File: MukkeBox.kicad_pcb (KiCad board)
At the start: 4 copper layers, 291 parts, among them J101 ST_Link_V2_10P, J102 Jumper, J103 Jumper, J104 Jumper, J105 Jumper, J106 Jumper, J107 PinHeader, J108 PinHeader, J201 TB001-500-07BE CUI_Devices, J401 TB001-500-02BE CUI_Devices, J501 TB001-500-04BE CUI_Devices, J601 Conn_01x03_Female, J602 Conn_02x01, J801 Conn_01x04, J802 Conn_01x04, Q101 NTK3043N, Q201 NTD14N03RT4G, Q202 NTD14N03RT4G, Q203 NTD14N03RT4G, Q301 MMBT2222LT1G, Q302 TK7R7P10PL, Q401 NTK3043N, Q402 FDD4685-F085, SW101 Rotary_Encoder_Switch, SW501 DS04-254-2-02BK-SMT, U101 TPS7B82-Q1, U102 STM32F030C6Tx_MukkeBox, U201 BQ76920, U202 BQ76200, U301 L7812, U302 UC3843_SOIC8, U401 MAX1873TEEE, U402 PC827, U501 TDA7498L, U601 XC6216C, U602 TDA7418, U701 XS3868, U801 MCP23017_SO, Y101 FOXSDLF/080-20

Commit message: Balancer geplaced
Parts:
- J401: moved to F.Cu
- moved J201 356.0 mm to (38.4, 114.2), turned to 90 degrees
- moved C203 355.9 mm to (47.3, 105.9), turned to 180 degrees
- moved R210 350.6 mm to (59.7, 110.9)
- moved D201 348.4 mm to (70.0, 109.6)
- moved C212 345.8 mm to (77.7, 103.1), turned to 270 degrees
- moved R215 345.0 mm to (90.5, 121.1)
- moved R206 341.3 mm to (59.1, 116.7)
- moved R205 341.0 mm to (47.3, 115.4)
- moved Q202 340.5 mm to (90.7, 109.9), turned to 90 degrees
- moved R207 338.6 mm to (40.0, 119.8), turned to 180 degrees
- moved C207 335.8 mm to (61.0, 115.0), turned to 180 degrees
- moved C204 334.6 mm to (47.3, 110.9), turned to 180 degrees
- moved R204 334.4 mm to (47.3, 109.2), turned to 180 degrees
- moved C205 334.0 mm to (47.3, 113.7), turned to 180 degrees
- moved R208 333.8 mm to (62.8, 116.7), turned to 180 degrees
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
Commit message: Step Up geplaced
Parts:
- moved R306 379.7 mm to (203.9, 60.2), turned to 90 degrees
- moved HS302 365.9 mm to (201.4, 45.2)
- moved R305 360.4 mm to (177.5, 63.9)
- moved R303 358.5 mm to (190.1, 60.6)
- moved C305 357.6 mm to (225.4, 35.7), turned to 270 degrees
- moved R302 356.3 mm to (185.3, 53.5), turned to 90 degrees
- moved R304 354.5 mm to (177.5, 62.1), turned to 180 degrees
- moved C306 353.4 mm to (190.1, 58.1)
- moved L301 351.9 mm to (172.9, 30.8)
- moved HS301 351.3 mm to (201.4, 24.2)
- moved R308 349.8 mm to (177.5, 58.9), turned to 180 degrees
- moved C302 347.0 mm to (183.7, 65.1)
- moved Q302 346.2 mm to (201.4, 48.6), turned to 90 degrees
- moved R301 345.1 mm to (177.5, 55.5), turned to 180 degrees
- moved Q301 343.5 mm to (182.1, 53.6)
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
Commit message: Alle Parts geplaced: Dimension der Platine 200x105qmm. TODO Anzeige überarbeiten
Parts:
- added C307: 560uF 50V, Capacitor_THT:CP_Radial_D12.5mm_P5.00mm, B.Cu at (117.1, 54.1)
- added C308: 560uF 50V, Capacitor_THT:CP_Radial_D12.5mm_P5.00mm, B.Cu at (175.1, 54.1)
- C301: value 1000u35V EEV-FK1V102V -> 560uF 50V; footprint Capacitor_SMD:CP_Elec_16x17.5 -> Capacitor_THT:CP_Radial_D12.5mm_P5.00mm; moved to B.Cu
- C305: value 1000u60V EEV-FK1V102V -> 560uF 50V; footprint Capacitor_SMD:CP_Elec_16x17.5 -> Capacitor_THT:CP_Radial_D12.5mm_P5.00mm; moved to B.Cu
- C525, C530, C531, C532, L501, L502, L503, L504: moved to B.Cu
- U102: footprint Package_QFP:LQFP-64_10x10mm_P0.5mm -> Package_QFP:LQFP-48_7x7mm_P0.5mm
- Y101: footprint Crystal:Crystal_SMD_HC49-SD_HandSoldering -> Crystal:Crystal_SMD_HC49-SD
- moved J501 278.4 mm to (240.8, 60.3), turned to 270 degrees
- moved R510 267.3 mm to (235.2, 88.6), turned to 90 degrees
- moved R511 267.2 mm to (234.9, 76.0), turned to 90 degrees
- moved U601 258.6 mm to (199.6, 117.1), turned to 180 degrees
- moved C525 258.4 mm to (211.4, 82.6), turned to 90 degrees
- moved C601 257.8 mm to (204.7, 118.1), turned to 180 degrees
- moved R601 255.4 mm to (194.8, 115.8), turned to 180 degrees
- moved R602 255.4 mm to (194.8, 119.1), turned to 180 degrees
- moved C612 254.9 mm to (185.9, 111.5), turned to 180 degrees
- moved C602 254.7 mm to (188.0, 117.3), turned to 270 degrees
- moved C528 254.6 mm to (235.2, 84.1), turned to 90 degrees
- moved C529 254.1 mm to (235.2, 80.5), turned to 90 degrees
- moved L503 253.2 mm to (224.8, 87.9)
- moved C523 251.9 mm to (233.5, 84.1), turned to 90 degrees
- moved R808 251.6 mm to (216.9, 137.7), turned to 180 degrees
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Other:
- board outline added: 200 x 105 mm

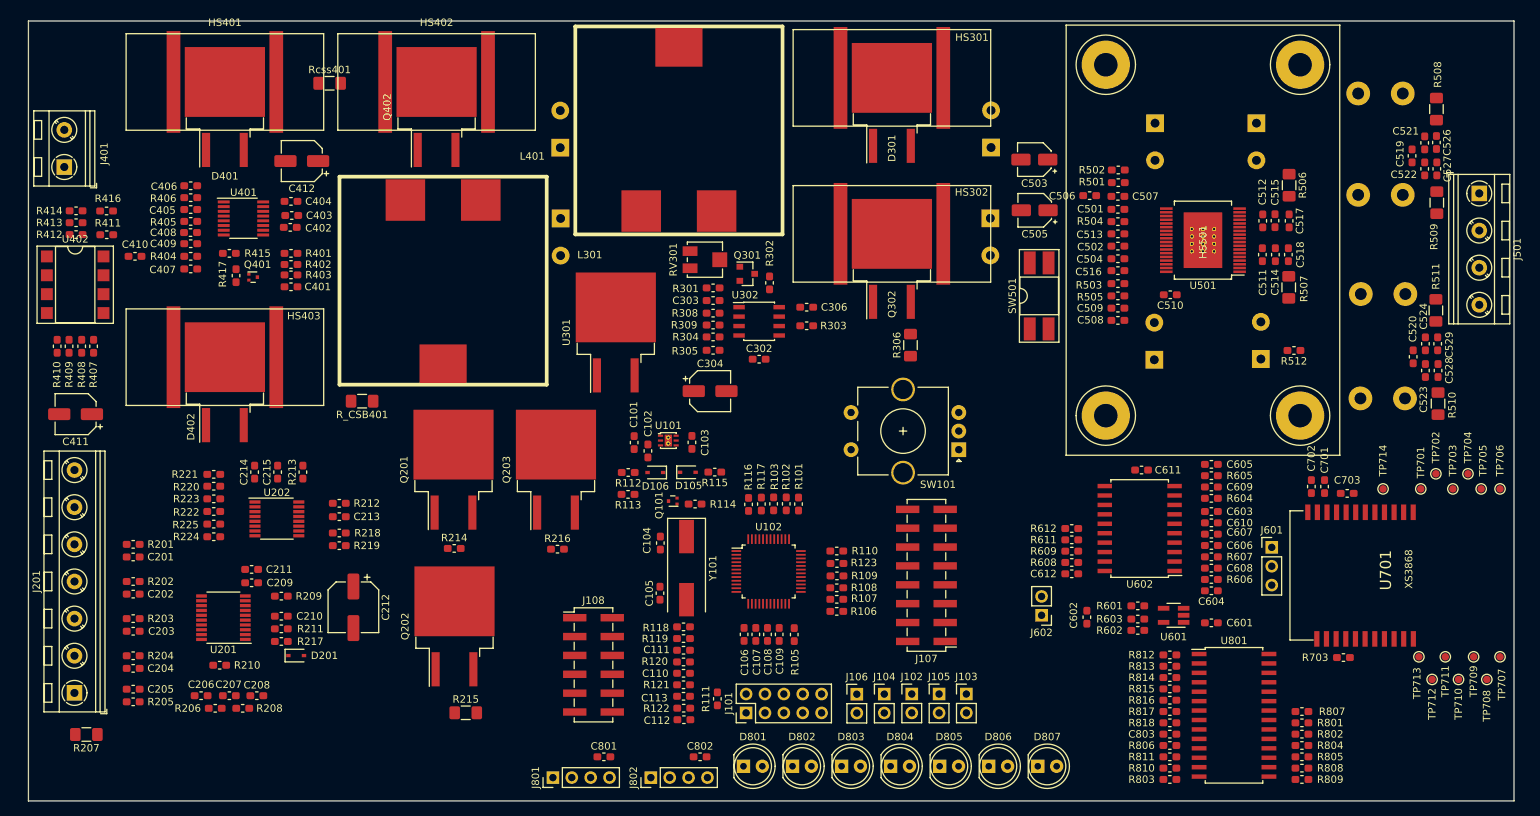
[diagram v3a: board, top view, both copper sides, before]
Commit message: Mountingholes und Heatsinks hinzugefügt
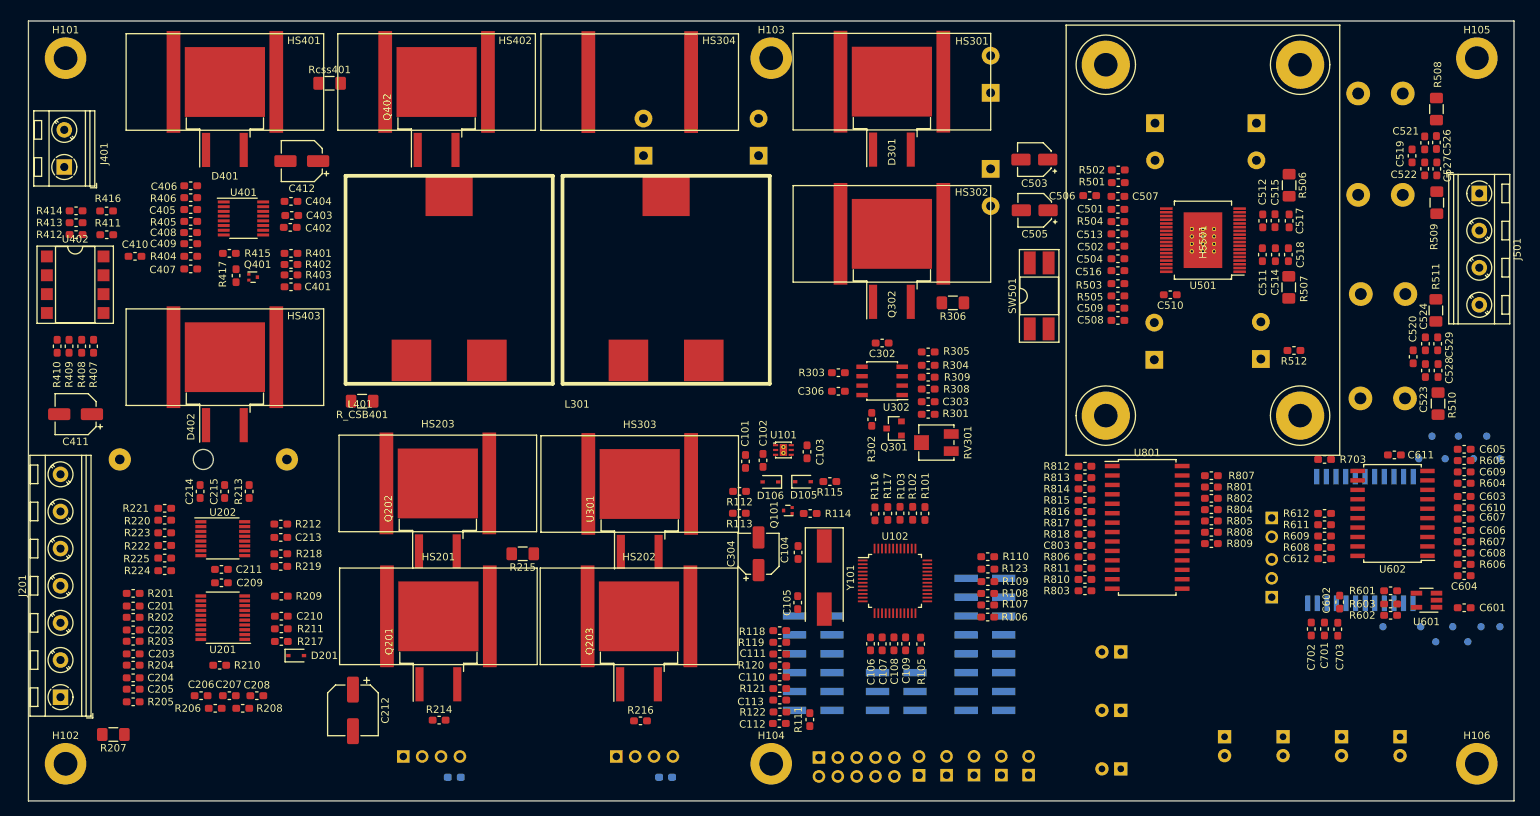
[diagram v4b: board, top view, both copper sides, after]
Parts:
- removed SW101: Rotary_Encoder_Switch, Rotary_Encoder:RotaryEncoder_Alps_EC11E-Switch_Vertical_H20mm_CircularMountingHoles
- added F201: Fuse, Fuse:Fuseholder_Cylinder-5x20mm_Schurter_0031_8201_Horizontal_Open, B.Cu at (80.3, 96.1)
- added H101: MountingHole_Pad, MountingHole:MountingHole_3.2mm_M3_DIN965_Pad, F.Cu at (50.5, 42.1)
- added H102: MountingHole_Pad, MountingHole:MountingHole_3.2mm_M3_DIN965_Pad, F.Cu at (50.5, 137.1)
- added H103: MountingHole_Pad, MountingHole:MountingHole_3.2mm_M3_DIN965_Pad, F.Cu at (145.5, 42.1)
- added H104: MountingHole_Pad, MountingHole:MountingHole_3.2mm_M3_DIN965_Pad, F.Cu at (145.5, 137.1)
- added H105: MountingHole_Pad, MountingHole:MountingHole_3.2mm_M3_DIN965_Pad, F.Cu at (240.5, 42.1)
- added H106: MountingHole_Pad, MountingHole:MountingHole_3.2mm_M3_DIN965_Pad, F.Cu at (240.5, 137.1)
- added HS201: Heatsink_Pad, Heatsink:Heatsink_AAVID_573300D00010G_TO-263, F.Cu at (100.7, 117.2)
- added HS202: Heatsink_Pad, Heatsink:Heatsink_AAVID_573300D00010G_TO-263, F.Cu at (127.7, 117.2)
- added HS203: Heatsink_Pad, Heatsink:Heatsink_AAVID_573300D00010G_TO-263, F.Cu at (100.6, 99.3)
- added HS303: Heatsink_Pad, Heatsink:Heatsink_AAVID_573300D00010G_TO-263, F.Cu at (127.8, 99.4)
- added HS304: Heatsink_Pad, Heatsink:Heatsink_AAVID_573300D00010G_TO-263, F.Cu at (127.8, 45.3)
- added J109: PinHeader, Connector_PinHeader_2.54mm:PinHeader_2x03_P2.54mm_Vertical_SMD, B.Cu at (162.3, 127.4)
- C801, C802, D801, D802, D803, D804, D805, D806, D807, J101, J102, J103, J104, J105, J106, J107, J108, J601, J602, J801, J802, TP701, TP702, TP703, TP704, TP705, TP706, TP707, TP708, TP709, TP710, TP711, TP712, TP713, TP714, U701: moved to B.Cu
- moved D801 88.5 mm to (230.1, 133.4), turned to 270 degrees
- moved D802 74.0 mm to (222.2, 133.4), turned to 270 degrees
- moved D803 59.6 mm to (214.4, 133.4), turned to 270 degrees
- moved D804 45.1 mm to (206.5, 133.4), turned to 270 degrees
- moved RV301 39.7 mm to (167.7, 93.8), turned to 270 degrees
- moved C601 34.1 mm to (238.8, 116.1)
- moved C602 34.1 mm to (222.0, 115.3)
- moved C603 34.1 mm to (238.8, 101.1)
- moved C604 34.1 mm to (238.8, 111.8)
- moved C605 34.1 mm to (238.8, 94.7)
- moved C606 34.1 mm to (238.8, 105.7)
- moved C607 34.1 mm to (238.8, 104.1)
- moved C608 34.1 mm to (238.8, 108.7)
- moved C609 34.1 mm to (238.8, 97.8)
- moved C610 34.1 mm to (238.8, 102.6)
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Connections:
- J201 pad 5: BATTERY+ -> /01_BMS/CELL4_SENSE
- R201 pad 2: BATTERY+ -> /01_BMS/CELL4_SENSE

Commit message: fertig zum routen
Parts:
- removed J102, J103, J105, J106: Jumper, Connector_PinHeader_2.54mm:PinHeader_1x02_P2.54mm_Vertical
- added J301: Conn_02x04_Odd_Even, Connector_PinHeader_2.54mm:PinHeader_2x04_P2.54mm_Vertical, B.Cu at (113.5, 54.3)
- added J302: Conn_02x04_Odd_Even, Connector_PinHeader_2.54mm:PinHeader_2x04_P2.54mm_Vertical, B.Cu at (186.5, 48.3)
- HS201, HS202, HS203, HS301, HS302, HS303, HS304: value Heatsink_Pad -> 573300D00000G
- J104: value Jumper -> Conn_02x05_Odd_Even; footprint Connector_PinHeader_2.54mm:PinHeader_1x02_P2.54mm_Vertical -> Connector_PinHeader_2.54mm:PinHeader_2x05_P2.54mm_Vertical_SMD
- J601: footprint Connector_PinHeader_2.54mm:PinHeader_1x03_P2.54mm_Vertical -> Connector_PinHeader_2.54mm:PinHeader_1x03_P2.54mm_Vertical_SMD_Pin1Left
- J602: footprint Connector_PinHeader_2.54mm:PinHeader_1x02_P2.54mm_Vertical -> Connector_PinHeader_2.54mm:PinHeader_1x02_P2.54mm_Vertical_SMD_Pin1Left
- J801: value Conn_01x04 -> Conn_01x05; footprint Connector_PinHeader_2.54mm:PinHeader_1x04_P2.54mm_Vertical -> Connector:1x04_P2.54mm_1.3OLED
- moved J801 114.6 mm to (208.2, 113.3), turned to 180 degrees
- moved J104 36.4 mm to (174.2, 102.6)
- moved D805 32.2 mm to (202.9, 107.3), turned to 270 degrees
- moved D806 22.8 mm to (195.0, 107.3), turned to 270 degrees
- moved R809 22.1 mm to (203.2, 129.4)
- moved C803 22.1 mm to (186.2, 129.7)
- moved R801 22.1 mm to (203.2, 121.8)
- moved R802 22.1 mm to (203.2, 123.3)
- moved R803 22.1 mm to (186.2, 135.8)
- moved R804 22.1 mm to (203.2, 124.9)
- moved R805 22.1 mm to (203.2, 126.4)
- moved R806 22.1 mm to (186.2, 131.2)
- moved R807 22.1 mm to (203.2, 120.3)
- moved R808 22.1 mm to (203.2, 127.9)
- moved R810 22.1 mm to (186.2, 134.3)
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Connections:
- C301 pad 1: SYSTEM_LOAD -> Net-(C301-Pad1)
- C305 pad 1: POWER_AMP -> Net-(C305-Pad1)
- C307 pad 1: SYSTEM_LOAD -> Net-(C301-Pad1)
- C308 pad 1: POWER_AMP -> Net-(C305-Pad1)
- C801 pad 1: +3V3 -> GND
- C801 pad 2: GND -> +3V3
- D301 pad 2: POWER_AMP -> Net-(C305-Pad1)
- HS301 pad 1: POWER_AMP -> Net-(C305-Pad1)
- J101 pad 7: Net-(J101-Pad7) -> /ST_Link_3V3
- J101 pad 8: Net-(J101-Pad7) -> /ST_Link_3V3
- J401 pad 1: GNDPWR -> GND
- J801 pad 1: SDA -> GND
- J801 pad 2: SCL -> +3V3
- J801 pad 3: +3V3 -> SCL
- J801 pad 4: GND -> SDA
- L301 pad 1: SYSTEM_LOAD -> Net-(C301-Pad1)
- R304 pad 2: SYSTEM_LOAD -> Net-(C301-Pad1)
- RV301 pad 1: POWER_AMP -> Net-(C305-Pad1)
- U102 pad 22: Net-(J102-Pad1) -> Net-(J104-Pad3)
- U102 pad 30: Net-(J105-Pad1) -> Net-(J104-Pad5)
- U102 pad 31: Net-(J103-Pad1) -> Net-(J104-Pad7)
- U301 pad 1: SYSTEM_LOAD -> Net-(C301-Pad1)
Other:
- net class Default: clearance 0.2 -> 0.15
- rule trace_clearance: 0.2 -> 0.15
- rule trace_min: 0.2 -> 0.15
- rule via_min_drill: 0.3 -> 0.2
- rule via_min_size: 0.4 -> 0.3

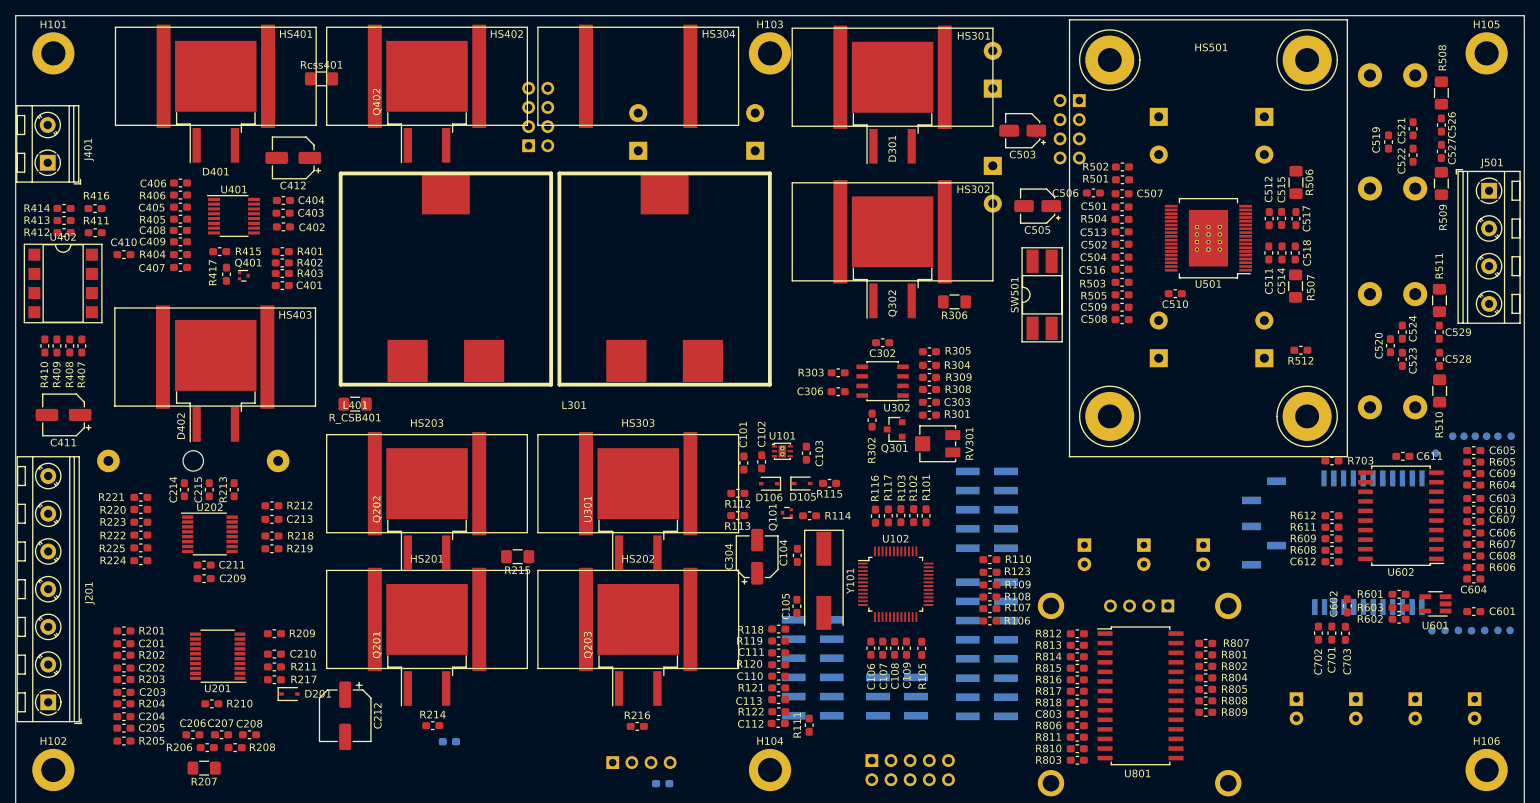
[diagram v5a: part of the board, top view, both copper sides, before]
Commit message: Amp verdrahtet, Einige Layers verlegt
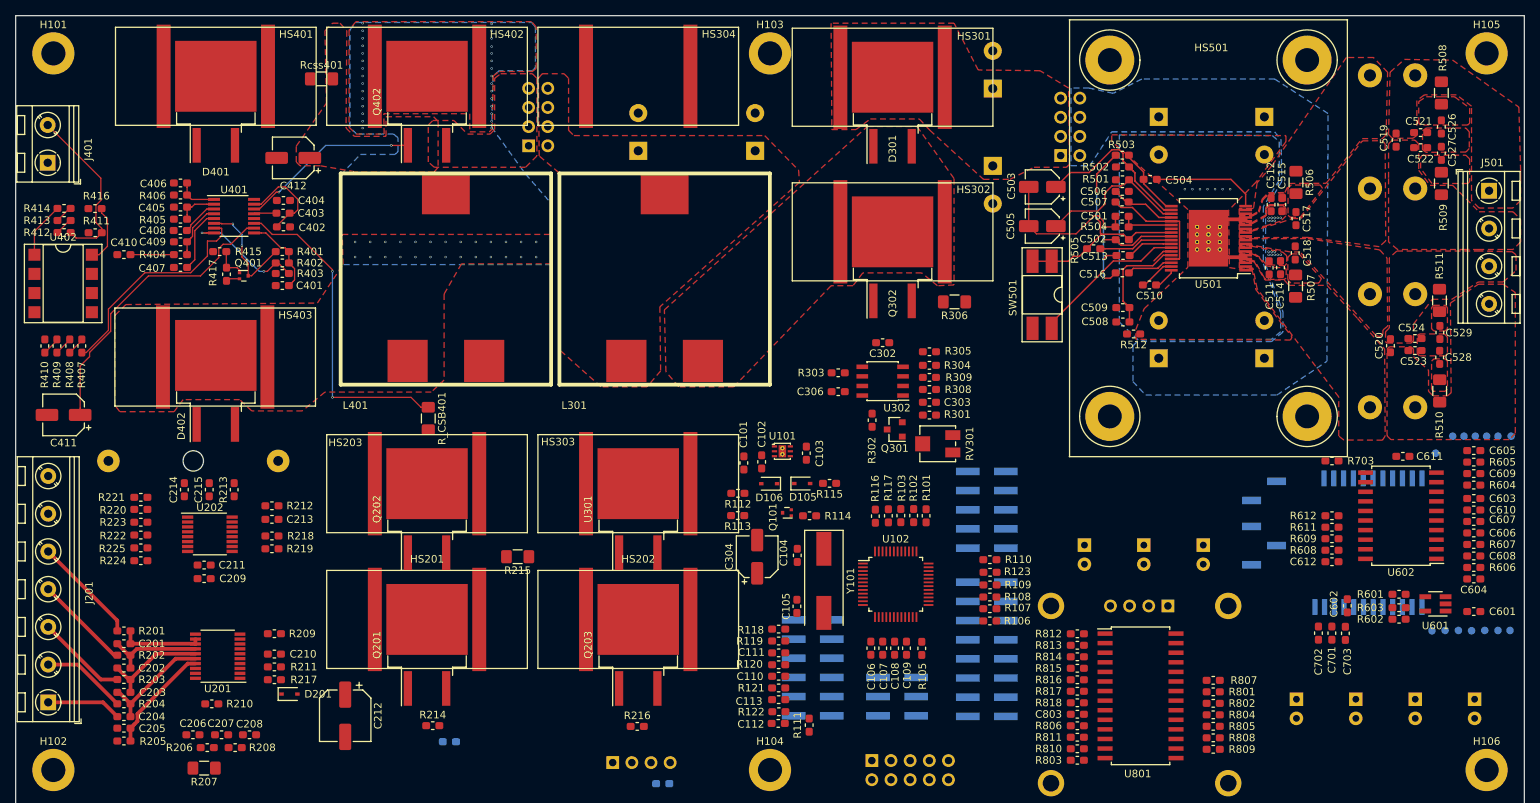
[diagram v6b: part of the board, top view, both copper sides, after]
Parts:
- moved R512 22.3 mm to (193.7, 79.3)
- moved R503 16.9 mm to (192.2, 55.6)
- moved C504 11.0 mm to (195.9, 58.8)
- moved R_CSB401 9.88 mm to (100.2, 90.5), turned to 270 degrees
- moved C503 7.89 mm to (181.6, 59.8)
- moved J302 7.71 mm to (184.0, 55.6), turned to 0 degrees
- moved R505 7.18 mm to (188.4, 68.0)
- moved R802 5.00 mm to (204.2, 128.2)
- moved R804 5.00 mm to (204.2, 129.8)
- moved R805 5.00 mm to (204.2, 131.3)
- moved R808 5.00 mm to (204.2, 132.8)
- moved R809 5.00 mm to (204.2, 134.3)
- moved R801 5.00 mm to (204.2, 126.7)
- moved R807 5.00 mm to (204.2, 125.2)
- moved C506 3.83 mm to (192.2, 60.4), turned to 180 degrees
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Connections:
- J501 pad 3: /Amplifier/SPEAKER_R+ -> /Amplifier/SPEAKER_R-
- J501 pad 4: /Amplifier/SPEAKER_R- -> /Amplifier/SPEAKER_R+
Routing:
- net Net-(L401-Pad2): track 0.00 -> 43.1 mm, vias 0 -> 2
- net GNDS: track 0.00 -> 41.3 mm, vias 0 -> 4
- net PACK+: track 0.00 -> 39.5 mm
- net /Amplifier/VDDS: track 0.00 -> 32.4 mm, vias 0 -> 2
- net /00_Charger/IOUT: track 0.00 -> 29.8 mm
- net Net-(Q402-Pad1): track 0.00 -> 23.9 mm, vias 0 -> 2
- net /00_Charger/DC_20V_POWER_SUPPLY: track 0.00 -> 22.5 mm
- net Net-(C503-Pad1): track 0.00 -> 21.9 mm
- net Net-(SW501-Pad4): track 0.00 -> 20.7 mm
- net Net-(C505-Pad1): track 0.00 -> 20.5 mm
- net Net-(R402-Pad1): track 0.00 -> 16.3 mm, vias 0 -> 2
- net GNDA: track 0.00 -> 15.6 mm
- net Net-(Q401-Pad3): track 0.00 -> 15.2 mm, vias 0 -> 2
- net /01_BMS/V_CELL1: track 0.00 -> 15.2 mm
- net Net-(C508-Pad2): track 0.00 -> 14.5 mm
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- added copper zone on F.Cu, net /Amplifier/SPEAKER_L+
- added copper zone on F.Cu, net /Amplifier/SPEAKER_L-
- added copper zone on F.Cu, net /Amplifier/SPEAKER_R+
- added copper zone on F.Cu, net /Amplifier/SPEAKER_R-
- added copper zone on B.Cu, net GNDPWR
- added copper zone on F.Cu, net GNDPWR
- added copper zone on F.Cu, net Net-(C301-Pad1)
- added copper zone on F.Cu, net Net-(C305-Pad1)
- added copper zone on F.Cu, net Net-(C517-Pad1)
- added copper zone on F.Cu, net Net-(C517-Pad2)
- added copper zone on F.Cu, net Net-(C518-Pad1)
- added copper zone on F.Cu, net Net-(C518-Pad2)
- added copper zone on F.Cu, net Net-(C526-Pad1)
- added copper zone on F.Cu, net Net-(C527-Pad2)
- added copper zone on F.Cu, net Net-(C528-Pad1)
- added copper zone on F.Cu, net Net-(C529-Pad2)
- added copper zone on F.Cu, net Net-(D301-Pad1)
- added copper zone on B.Cu, net Net-(D402-Pad2)
- added copper zone on F.Cu, net Net-(D402-Pad2)
- added copper zone on F.Cu, net Net-(L501-Pad1)
- added copper zone on F.Cu, net Net-(L503-Pad1)
- added copper zone on B.Cu, net POWER_AMP
- added copper zone on F.Cu, net POWER_AMP
- added copper zone on F.Cu, net SYSTEM_LOAD
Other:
- copper layers 4 -> 2
- net class Default: trace_width 0.25 -> 0.15; via_dia 0.8 -> 0.3; via_drill 0.4 -> 0.2
- rule trace_min: 0.15 -> 0.1
